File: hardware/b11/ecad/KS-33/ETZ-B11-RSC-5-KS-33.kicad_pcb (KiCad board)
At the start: 2 copper layers, 112.3 x 85.8 mm, 0 parts

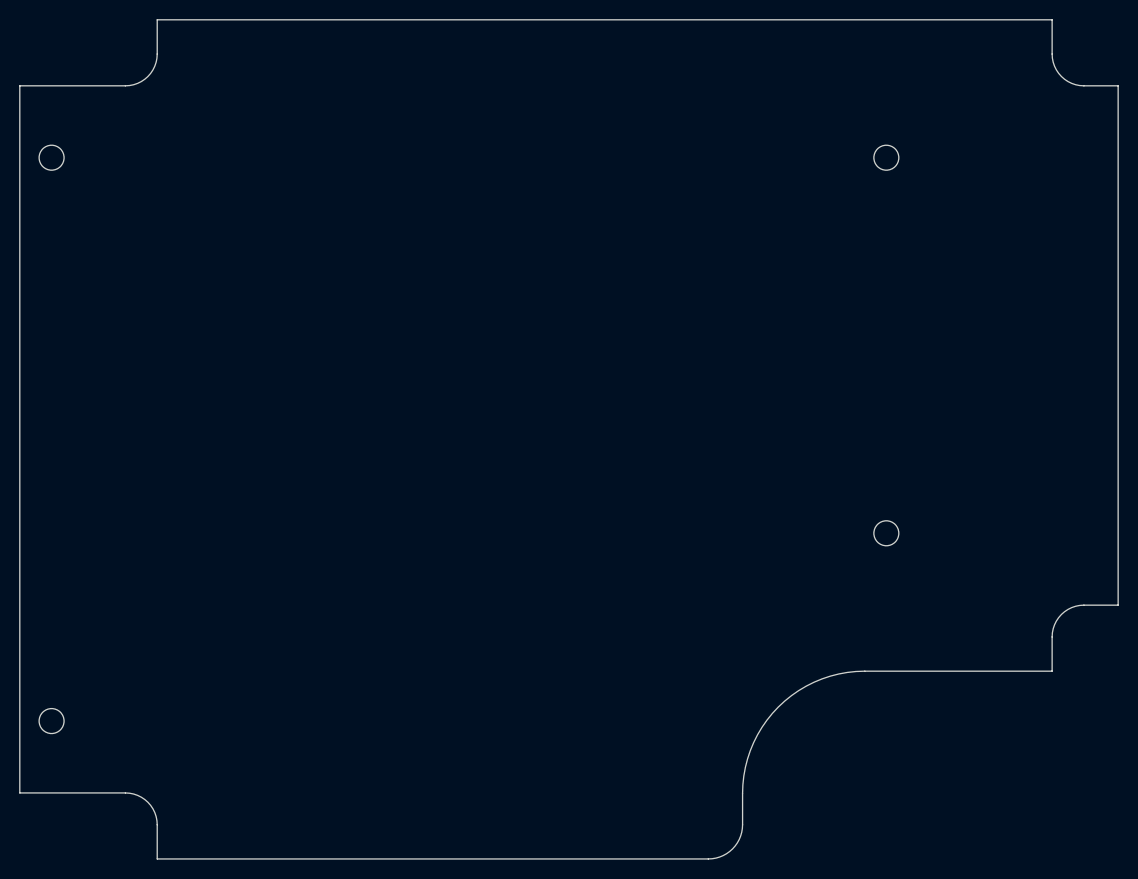
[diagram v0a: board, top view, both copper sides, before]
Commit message: fix(hardware/b11): fix 3D model paths, .kicad_pro files, KS-33 placement
- Update footprint model paths to \${KIPRJMOD}/../../../../lib/3d-models/
  so 3D models resolve correctly from ecad/{family}/ project directories
- Generate .kicad_pro for all 24 boards; remove dangling old ecad/ root .kicad_pro files
- Fix place-switch-sockets.py and place-switch-leds.py to read grid origin
  from board design settings instead of config constants
- Place KS-33 switch sockets and LEDs on all 4 carrier boards
- Propagate KiCad-normalised 1.6mm stackup across KS-33 SC boards

Co-Authored-By: Claude Sonnet 4.6 <noreply@anthropic.com>
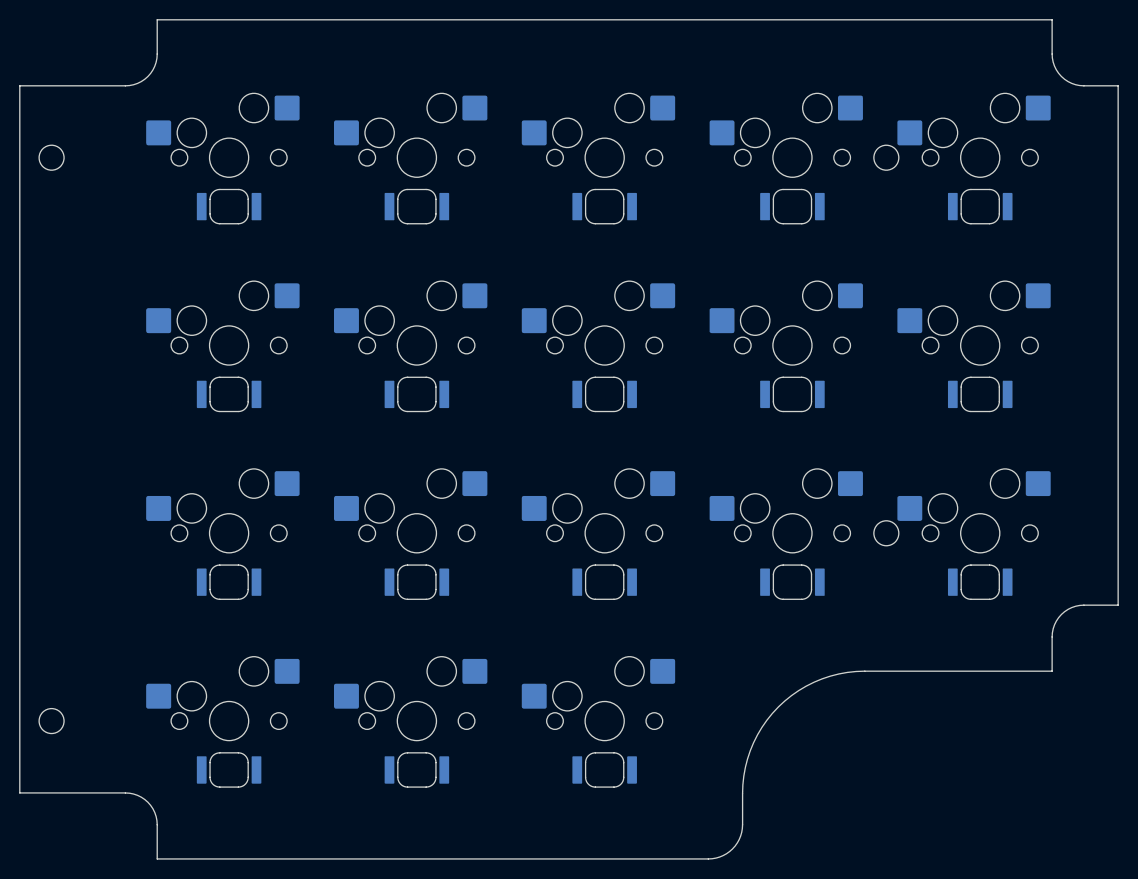
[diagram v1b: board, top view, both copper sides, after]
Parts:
- added LED1: 6028_LED, 6028_LED, F.Cu at (190.6, 78.3)
- added LED10: 6028_LED, 6028_LED, F.Cu at (113.8, 97.5)
- added LED11: 6028_LED, 6028_LED, F.Cu at (190.6, 116.7)
- added LED12: 6028_LED, 6028_LED, F.Cu at (171.3, 116.7)
- added LED13: 6028_LED, 6028_LED, F.Cu at (152.2, 116.7)
- added LED14: 6028_LED, 6028_LED, F.Cu at (132.9, 116.7)
- added LED15: 6028_LED, 6028_LED, F.Cu at (113.8, 116.7)
- added LED16: 6028_LED, 6028_LED, F.Cu at (152.2, 135.9)
- added LED17: 6028_LED, 6028_LED, F.Cu at (132.9, 135.9)
- added LED18: 6028_LED, 6028_LED, F.Cu at (113.8, 135.9)
- added LED2: 6028_LED, 6028_LED, F.Cu at (171.3, 78.3)
- added LED3: 6028_LED, 6028_LED, F.Cu at (152.2, 78.3)
- added LED4: 6028_LED, 6028_LED, F.Cu at (132.9, 78.3)
- added LED5: 6028_LED, 6028_LED, F.Cu at (113.8, 78.3)
- added LED6: 6028_LED, 6028_LED, F.Cu at (190.6, 97.5)
- added LED7: 6028_LED, 6028_LED, F.Cu at (171.3, 97.5)
- added LED8: 6028_LED, 6028_LED, F.Cu at (152.2, 97.5)
- added LED9: 6028_LED, 6028_LED, F.Cu at (132.9, 97.5)
- added SW1: KS-2P02B01-01-a, KS-2P02B01-01-a, F.Cu at (190.6, 73.3)
- added SW10: KS-2P02B01-01-a, KS-2P02B01-01-a, F.Cu at (113.8, 92.5)
- added SW11: KS-2P02B01-01-a, KS-2P02B01-01-a, F.Cu at (190.6, 111.7)
- added SW12: KS-2P02B01-01-a, KS-2P02B01-01-a, F.Cu at (171.3, 111.7)
- added SW13: KS-2P02B01-01-a, KS-2P02B01-01-a, F.Cu at (152.2, 111.7)
- added SW14: KS-2P02B01-01-a, KS-2P02B01-01-a, F.Cu at (132.9, 111.7)
- added SW15: KS-2P02B01-01-a, KS-2P02B01-01-a, F.Cu at (113.8, 111.7)
- added SW16: KS-2P02B01-01-a, KS-2P02B01-01-a, F.Cu at (152.2, 130.9)
- added SW17: KS-2P02B01-01-a, KS-2P02B01-01-a, F.Cu at (132.9, 130.9)
- added SW18: KS-2P02B01-01-a, KS-2P02B01-01-a, F.Cu at (113.8, 130.9)
- added SW2: KS-2P02B01-01-a, KS-2P02B01-01-a, F.Cu at (171.3, 73.3)
- added SW3: KS-2P02B01-01-a, KS-2P02B01-01-a, F.Cu at (152.2, 73.3)
- added SW4: KS-2P02B01-01-a, KS-2P02B01-01-a, F.Cu at (132.9, 73.3)
- added SW5: KS-2P02B01-01-a, KS-2P02B01-01-a, F.Cu at (113.8, 73.3)
- added SW6: KS-2P02B01-01-a, KS-2P02B01-01-a, F.Cu at (190.6, 92.5)
- added SW7: KS-2P02B01-01-a, KS-2P02B01-01-a, F.Cu at (171.3, 92.5)
- added SW8: KS-2P02B01-01-a, KS-2P02B01-01-a, F.Cu at (152.2, 92.5)
- added SW9: KS-2P02B01-01-a, KS-2P02B01-01-a, F.Cu at (132.9, 92.5)
